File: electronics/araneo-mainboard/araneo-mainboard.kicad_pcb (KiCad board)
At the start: 2 copper layers, 71.5 x 68.5 mm, 97 parts, among them IC1 TPS54302DDCR, IC2 BMI270, IC3 MMC5983MA, J2 OLED, J3 GPIO, SW2 SW, SW3 SW, U4 POWER, U5 PAM8403D, U6 3V3

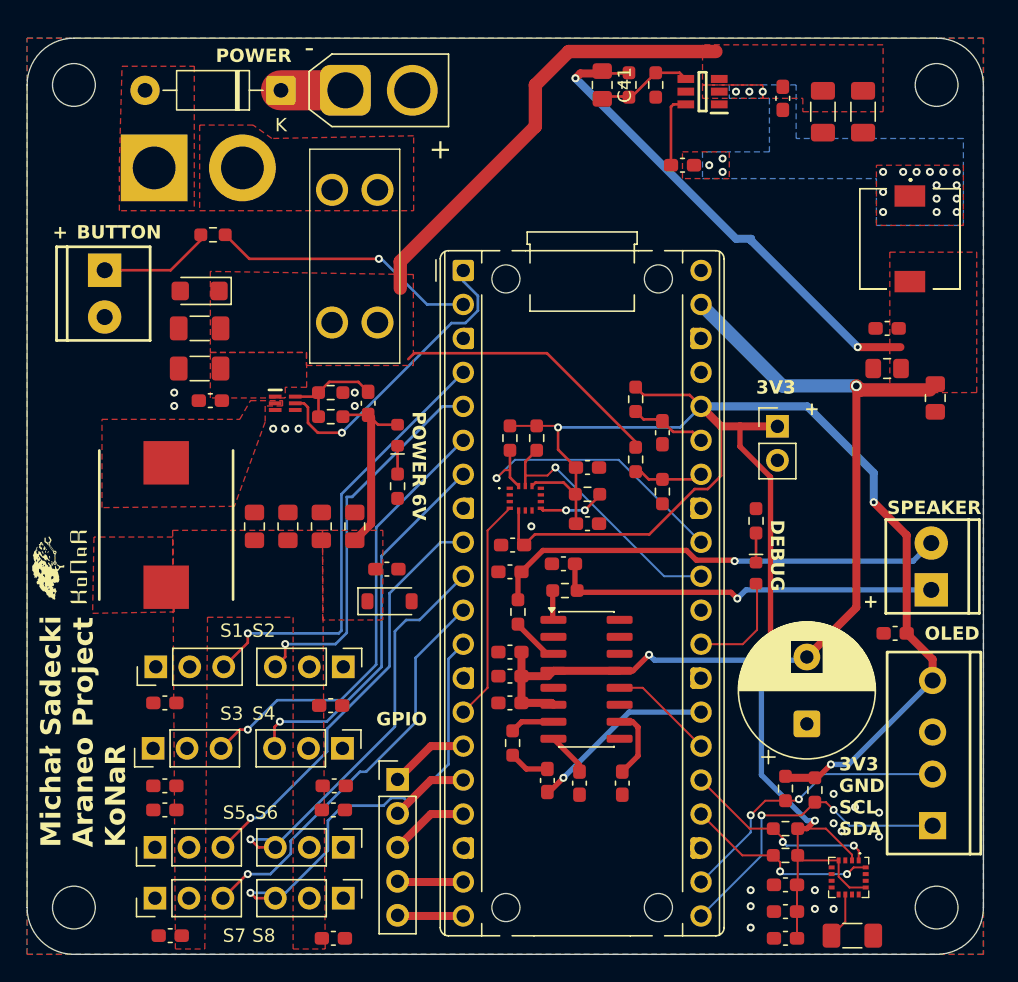
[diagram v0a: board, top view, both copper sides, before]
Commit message: electronics: remove unnecessary capacitors, add net labels, change screw terminal to JST_XH
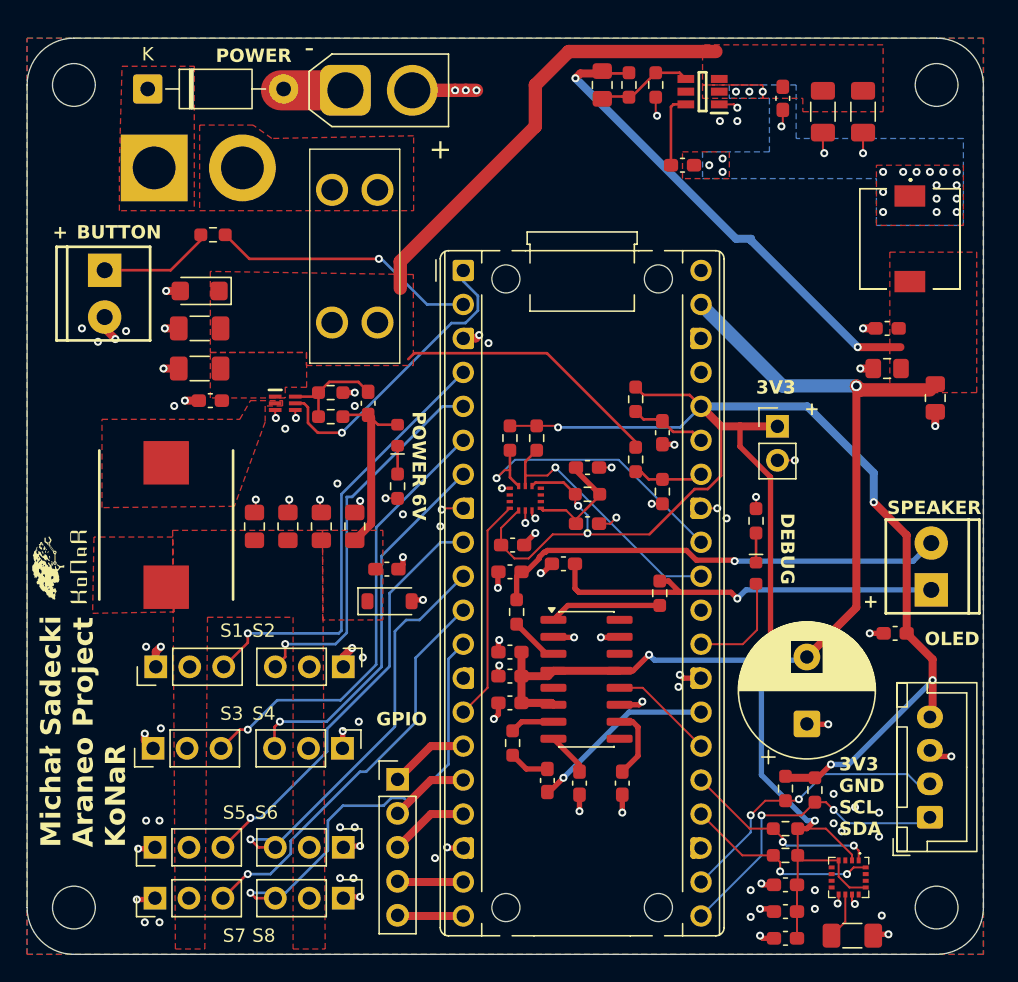
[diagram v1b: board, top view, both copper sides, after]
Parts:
- removed C21, C22, C23, C24, C25, C26, C27, C28: 0.1uF, Capacitor_SMD:C_0603_1608Metric_Pad1.08x0.95mm_HandSolder
- removed FB1, FB2: FerriteBead, Resistor_SMD:R_0603_1608Metric_Pad0.98x0.95mm_HandSolder
- added R20: 0, Resistor_SMD:R_0603_1608Metric_Pad0.98x0.95mm_HandSolder, F.Cu at (138.8, 77.0)
- added R21: 0, Resistor_SMD:R_0603_1608Metric_Pad0.98x0.95mm_HandSolder, F.Cu at (128.1, 78.4)
- J2: footprint PCM_SparkFun-Connector:ScrewTerminal_1x04_P3.5mm_Locking -> Connector_JST:JST_XH_B4B-XH-A_1x04_P2.50mm_Vertical
- R13: value 1.2k -> 1k
- moved D6 9.96 mm to (100.5, 39.3), turned to 0 degrees
- moved J2 0.49 mm to (159.0, 93.8)
- turned C1 to 180 degrees
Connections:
- net Net-(C11-Pad2) renamed /SP_P_O
- net Net-(C12-Pad2) renamed /SP_N_O
- net Net-(C13-Pad2) renamed /INL_R
- net Net-(D3-K) renamed /D_LED
- net Net-(D5-K) renamed /LED6
- net Net-(IC1-BOOT) renamed /BOOT
- net Net-(IC1-FB) renamed /FB5
- net Net-(IC1-SW) renamed /SW5_L
- net Net-(IC3-CAP) renamed /Magnetometer/MAG_CAP
- net Net-(PS1-FB) renamed /FB6
- net Net-(PS1-SW) renamed /SW6_L
- net Net-(SW2-A) renamed /BTN_R
- net Net-(SW3-B) renamed /VBAT_SW
- net Net-(U5-INR) renamed /INR
- net Net-(U5-VREF) renamed /SP_VREF
- C42 pad 2: +3V3 -> /IMU/VDD_IMU
- C43 pad 2: +3V3 -> /IMU/VDD_IMU
- D6 pad 1: +7.4V -> /VBAT_D
- D6 pad 2: Net-(D6-A) -> +7.4V
- FB4 pad 1: Net-(IC2-VDD) -> /IMU/VDD_IMU
- IC2 pad 8: Net-(IC2-VDD) -> /IMU/VDD_IMU
- SW3 pad 1: Net-(D6-A) -> /VBAT_D
- U5 pad 1: Net-(U5-LOUT+) -> /LOUT+
- U5 pad 3: Net-(U5-LOUT-) -> /LOUT-
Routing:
- net GND: track 0.00 -> 81.6 mm, vias 20 -> 106
- net /IMU/VDD_IMU: track 0.00 -> 8.93 mm
- net /LOUT+: track 0.00 -> 8.40 mm
- net Net-(IC2-VDD): track 5.01 -> 0.00 mm, vias 2 -> 0
- net /LOUT-: track 0.00 -> 3.67 mm
- net Net-(U5-LOUT-): track 3.60 -> 0.00 mm
- net Net-(U5-LOUT+): track 2.21 -> 0.00 mm
- net /SP_P_O: track 29.1 -> 30.9 mm
- net +3V3: track 162.5 -> 163.9 mm, vias 5 -> 8
- added copper zone on F.Cu, net /VBAT_D
- removed copper zone on F.Cu, net Net-(D6-A)

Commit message: electronics: change bucks layout
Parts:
- moved konar1 66.7 mm to (152.2, 42.5), turned to 0 degrees
- moved C41 29.2 mm to (161.8, 49.5), turned to 90 degrees
- moved R16 25.3 mm to (159.5, 49.5), turned to -90 degrees
- moved R17 17.2 mm to (154.2, 46.0), turned to 0 degrees
- moved IC1 16.1 mm to (154.2, 50.0), turned to 0 degrees
- moved R14 16.1 mm to (120.0, 57.0), turned to -90 degrees
- moved C20 15.6 mm to (154.0, 52.8), turned to 0 degrees
- moved D6 13.3 mm to (96.4, 52.0)
- moved SW2 13.2 mm to (95.8, 66.0)
- moved SW3 12.8 mm to (98.5, 57.8)
- moved C31 12.1 mm to (100.8, 68.8), turned to -90 degrees
- moved D2 10.3 mm to (106.5, 64.5), turned to 90 degrees
- moved C45 10.2 mm to (114.2, 84.5)
- moved R6 10.0 mm to (114.0, 72.0)
- moved D1 9.93 mm to (114.8, 86.8)
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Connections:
- net /IMU/VDD_IMU renamed /VDD_IMU
- net /Magnetometer/MAG_CAP renamed /MAG_CAP
- net Net-(U5-INL) renamed /INL
- IC2 pad 13: /IMU_SDA -> /IMU_SCL
- IC2 pad 14: /IMU_SCL -> /IMU_SDA
- R1 pad 2: /IMU_SDA -> /IMU_SCL
- R2 pad 2: /IMU_SCL -> /IMU_SDA
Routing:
- net +5V: track 106.9 -> 28.5 mm, vias 4 -> 1
- net +3V3: track 163.9 -> 123.1 mm
- net GND: track 81.6 -> 41.9 mm, vias 106 -> 50
- net +7.4V_F: track 55.1 -> 20.3 mm
- net /BUTTON: track 20.0 -> 0.00 mm, vias 1 -> 0
- net /PWM6: track 30.3 -> 14.0 mm, vias 1 -> 0
- net /PWM8: track 31.9 -> 15.9 mm, vias 1 -> 0
- net /PWM7: track 30.3 -> 15.1 mm, vias 1 -> 0
- net +6V: track 14.4 -> 0.00 mm
- net /PWM3: track 33.7 -> 19.5 mm, vias 1 -> 0
- net /PWM5: track 31.7 -> 19.2 mm, vias 1 -> 0
- net /PWM1: track 33.4 -> 23.1 mm, vias 1 -> 0
- net /BTN_R: track 8.52 -> 0.00 mm
- net /FB6: track 8.01 -> 0.00 mm
- net /PWM2: track 28.6 -> 21.3 mm, vias 1 -> 0
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- removed copper zone on F.Cu, net +5V
- removed copper zone on F.Cu, net +7.4V_F
- removed copper zone on B.Cu, net /SW5_L
- removed copper zone on F.Cu, net /SW5_L
- removed copper zone on F.Cu, net /SW6_L
- removed copper zone on F.Cu, net /VBAT_D
- removed copper zone on F.Cu, net /VBAT_SW
- removed copper zone on B.Cu, net GND
- removed copper zone on F.Cu, net GND
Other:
- board size 71.5 x 68.5 mm -> 71.5 x 63.8 mm

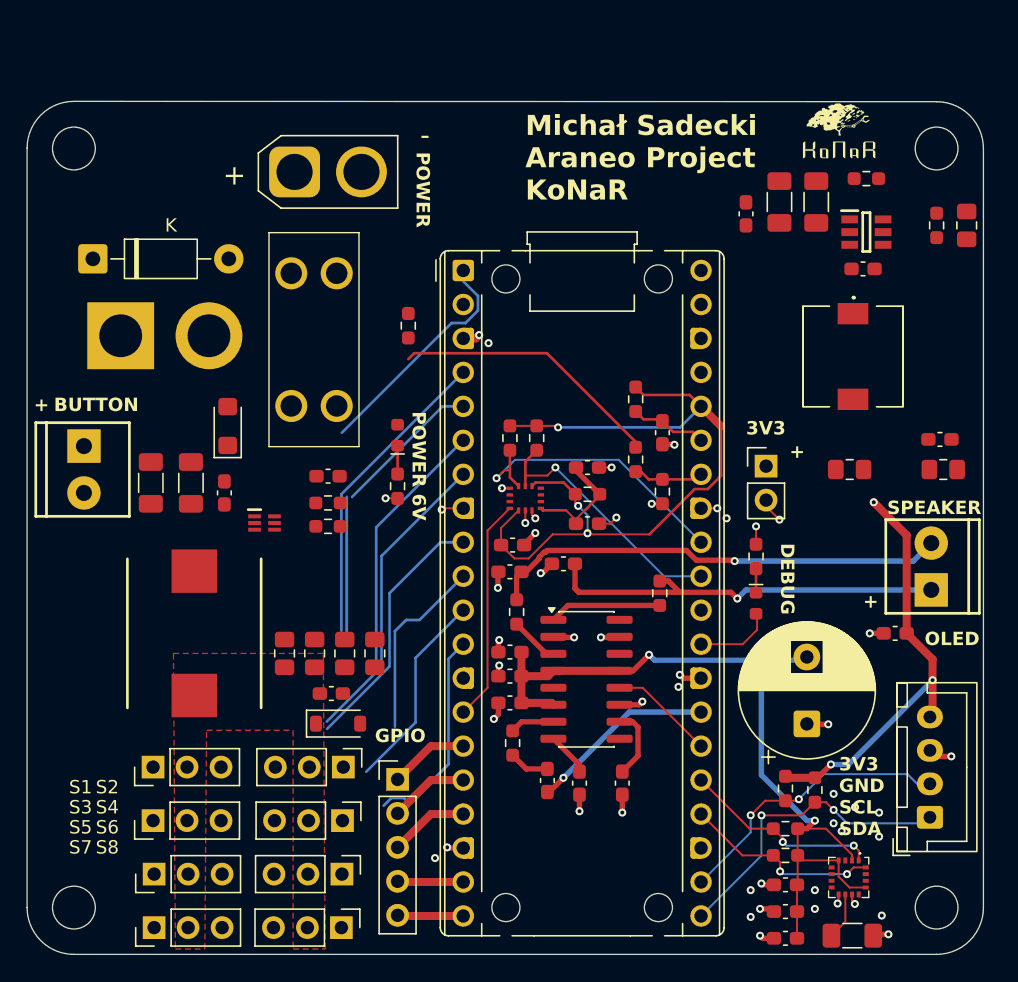
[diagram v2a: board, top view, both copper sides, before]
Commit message: electronics: connect bucks
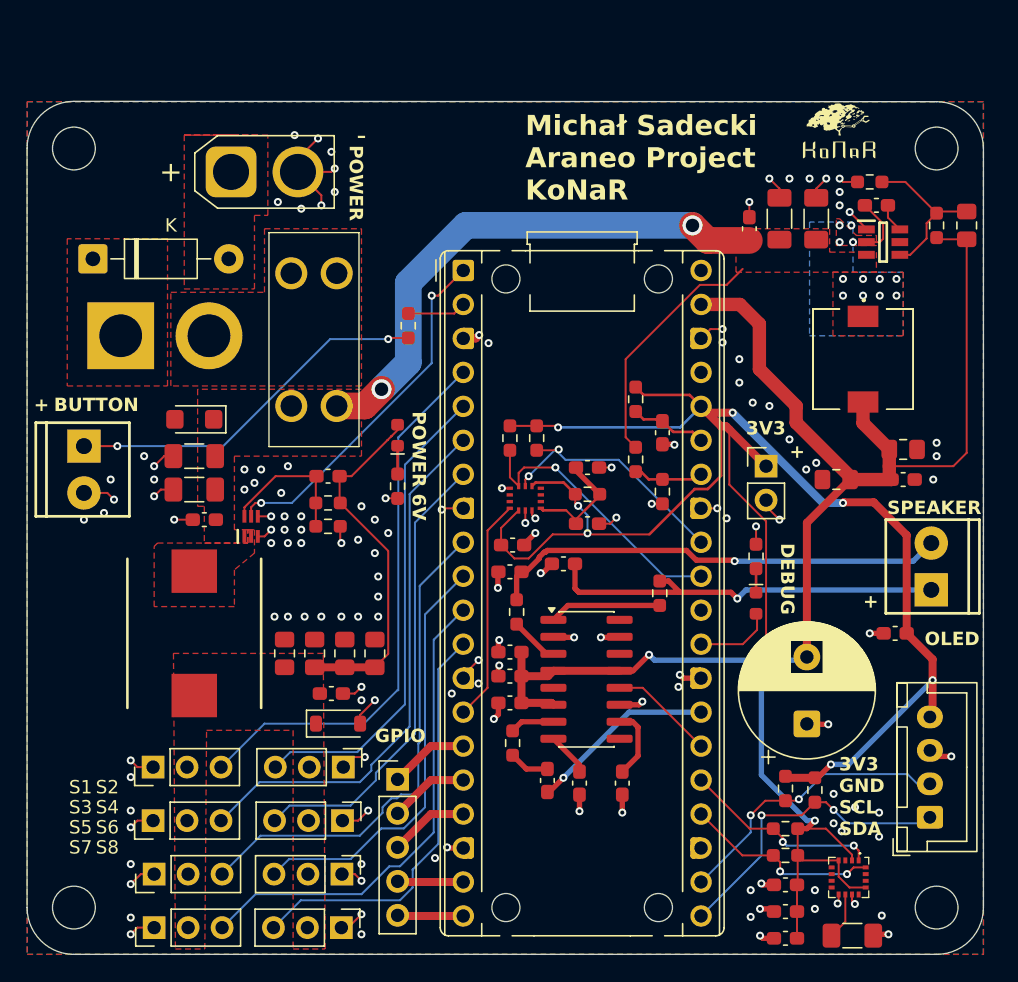
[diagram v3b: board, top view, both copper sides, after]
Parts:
- moved C29 8.04 mm to (152.0, 68.5), turned to 180 degrees
- moved C20 4.85 mm to (155.0, 48.0)
- moved U4 4.75 mm to (106.8, 45.5)
- moved C30 4.27 mm to (157.0, 66.2), turned to 0 degrees
- moved C44 4.07 mm to (157.0, 68.5)
- moved C31 3.82 mm to (104.0, 66.8), turned to 180 degrees
- moved D2 2.55 mm to (104.0, 64.0), turned to 180 degrees
- moved C33 2.50 mm to (104.8, 71.5), turned to 180 degrees
- moved IC1 1.46 mm to (155.5, 50.8)
- moved C39 1.25 mm to (147.8, 49.0)
- moved C40 1.25 mm to (150.5, 49.0)
- moved C35 1.14 mm to (145.5, 49.8)
- moved PS1 1.03 mm to (108.2, 72.0), turned to 90 degrees
- moved L2 0.78 mm to (154.0, 59.5)
- moved C32 0.56 mm to (104.0, 69.2), turned to 180 degrees
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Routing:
- net +5V: track 28.5 -> 97.1 mm
- net GND: track 41.9 -> 92.8 mm, vias 50 -> 138
- net +3V3: track 123.1 -> 162.9 mm, vias 8 -> 9
- net +7.4V_F: track 20.3 -> 58.8 mm, vias 0 -> 2
- net /BTN_R: track 0.00 -> 27.6 mm, vias 0 -> 2
- net +6V: track 0.00 -> 26.9 mm
- net /PWM7: track 15.1 -> 36.3 mm
- net /PWM3: track 19.5 -> 40.3 mm
- net /PWM1: track 23.1 -> 41.4 mm
- net /PWM5: track 19.2 -> 37.4 mm
- net /PWM6: track 14.0 -> 31.8 mm
- net /PWM8: track 15.9 -> 31.4 mm
- net /PWM2: track 21.3 -> 35.7 mm
- net /FB5: track 0.00 -> 12.1 mm
- net /PWM4: track 22.7 -> 34.4 mm
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- added copper zone on F.Cu, net +7.4V
- added copper zone on F.Cu, net +7.4V_F
- added copper zone on B.Cu, net /SW5_L
- added copper zone on F.Cu, net /SW5_L
- added copper zone on F.Cu, net /SW6_L
- added copper zone on F.Cu, net /VBAT_D
- added copper zone on F.Cu, net /VBAT_SW
- added copper zone on B.Cu, net GND
- added copper zone on F.Cu, net GND

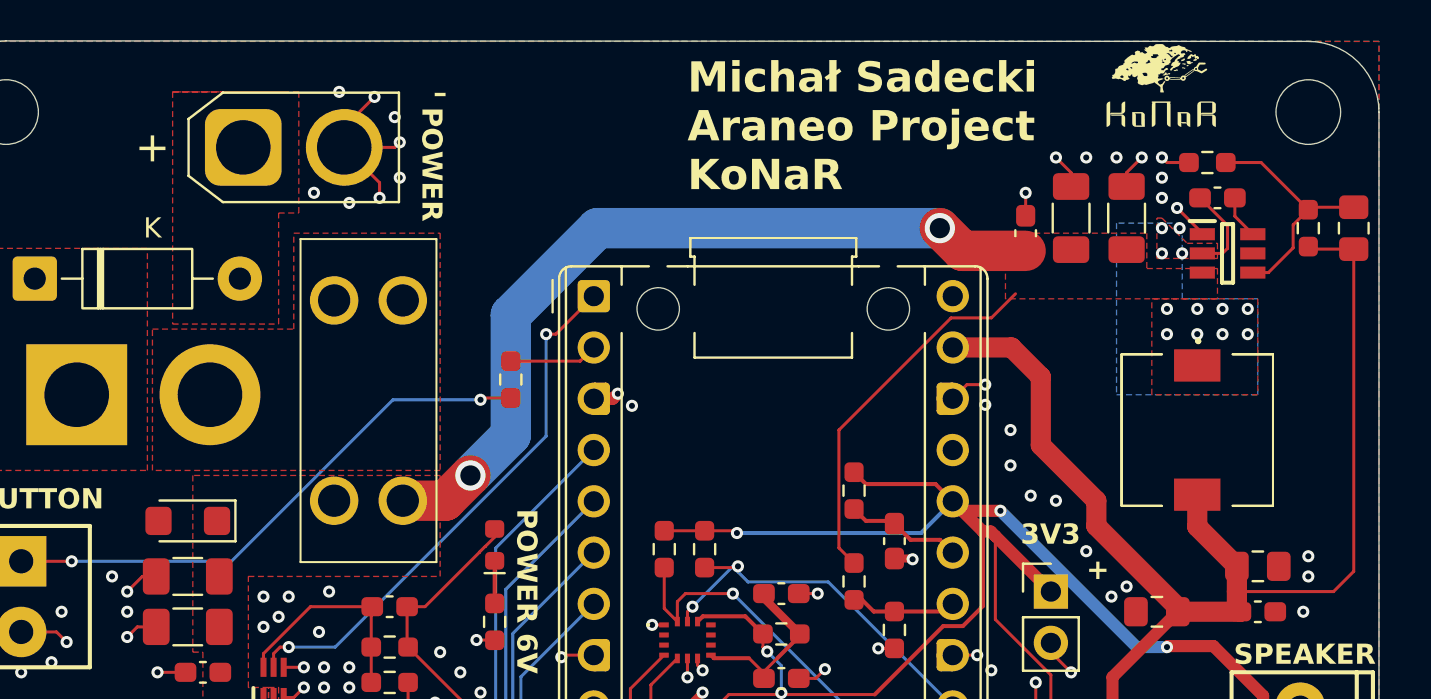
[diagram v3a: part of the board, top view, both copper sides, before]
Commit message: electronics: add vias
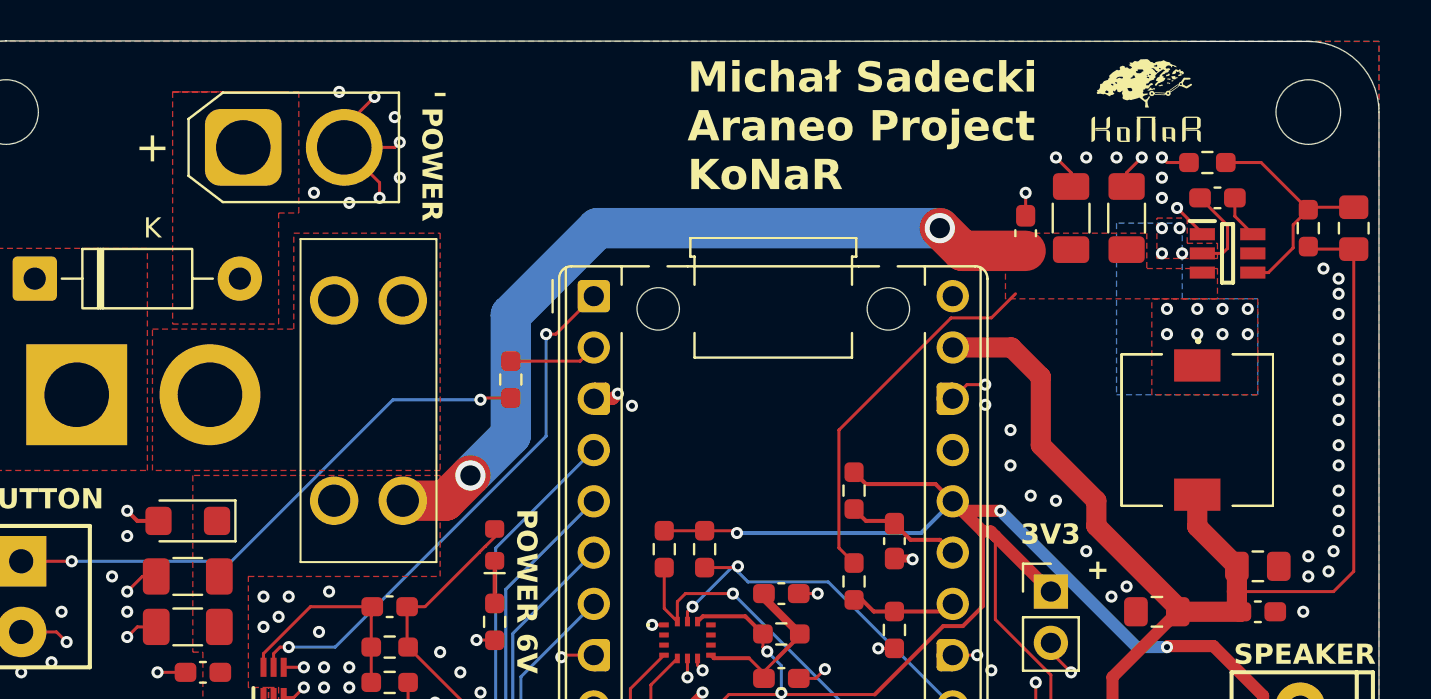
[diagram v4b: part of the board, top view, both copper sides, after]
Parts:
- moved konar1 1.06 mm to (151.5, 43.2)
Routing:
- net GND: track 92.8 -> 94.5 mm, vias 138 -> 156
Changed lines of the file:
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@@
 	(footprint "Custom:konar"
 		(layer "F.Cu")
-		(at 152.25 42.5)
+		(at 151.5 43.25)
 		(property "Reference" "konar1"
 			(at 0 0 0)
@@
 	)
 	(segment
+		(start 102.55 64)
+		(end 101.5 64)
+		(width 0.2)
+		(layer "F.Cu")
+		(net "GND")
+	)
+	(segment
 		(start 135.556587 71.343413)
 		(end 135.1 71.8)
@@
 	)
 	(segment
+		(start 101.5 64)
+		(end 101 63.5)
+		(width 0.2)
+		(layer "F.Cu")
+		(net "GND")
+	)
+	(segment
 		(start 143.1 70.65)
 		(end 141.89 70.65)
@@
 	)
 	(via
+		(at 161 61.25)
+		(size 0.6)
+		(drill 0.3)
+		(layers "F.Cu" "B.Cu")
+		(free yes)
+		(net "GND")
+	)
+	(via
 		(at 123.25 84.5)
 		(size 0.6)
@@
 	)
 	(via
+		(at 161 55)
+		(size 0.6)
+		(drill 0.3)
+		(layers "F.Cu" "B.Cu")
+		(free yes)
+		(net "GND")
+	)
+	(via
 		(at 99.25 94.5)
 		(size 0.6)
@@
 	)
 	(via
+		(at 160.5 66.5)
+		(size 0.6)
+		(drill 0.3)
+		(layers "F.Cu" "B.Cu")
+		(free yes)
+		(net "GND")
+	)
+	(via
+		(at 161 52)
+		(size 0.6)
+		(drill 0.3)
+		(layers "F.Cu" "B.Cu")
+		(free yes)
+		(net "GND")
+	)
+	(via
 		(at 107.75 67.75)
 		(size 0.6)
@@
 	)
 	(via
+		(at 161 59)
+		(size 0.6)
+		(drill 0.3)
+		(layers "F.Cu" "B.Cu")
+		(free yes)
+		(net "GND")
+	)
+	(via
 		(at 117.75 77.25)
 		(size 0.6)
@@
 	)
 	(via
+		(at 161 56)
+		(size 0.6)
+		(drill 0.3)
+		(layers "F.Cu" "B.Cu")
+		(free yes)
+		(net "GND")
+	)
+	(via
 		(at 151.8 92)
 		(size 0.6)
@@
 	)
 	(via
+		(at 160.25 51.5)
+		(size 0.6)
+		(drill 0.3)
+		(layers "F.Cu" "B.Cu")
+		(free yes)
+		(net "GND")
+	)
+	(via
 		(at 129.5 72.5)
 		(size 0.6)
@@
 	)
 	(via
+		(at 161 62.5)
+		(size 0.6)
+		(drill 0.3)
+		(layers "F.Cu" "B.Cu")
+		(free yes)
+		(net "GND")
+	)
+	(via
 		(at 143.1 70.65)
 		(size 0.6)
@@
 	)
 	(via
+		(at 161 64.5)
+		(size 0.6)
+		(drill 0.3)
+		(layers "F.Cu" "B.Cu")
+		(free yes)
+		(net "GND")
+	)
+	(via
 		(at 126.8 82.4)
 		(size 0.6)
@@
 	)
 	(via
+		(at 160.75 65.5)
+		(size 0.6)
+		(drill 0.3)
+		(layers "F.Cu" "B.Cu")
+		(free yes)
+		(net "GND")
+	)
+	(via
 		(at 110.25 47.75)
 		(size 0.6)
@@
 	)
 	(via
+		(at 101 64.75)
+		(size 0.6)
+		(drill 0.3)
+		(layers "F.Cu" "B.Cu")
+		(free yes)
+		(net "GND")
+	)
+	(via
 		(at 116.5 84)
 		(size 0.6)
@@
 	)
 	(via
+		(at 161 63.5)
+		(size 0.6)
+		(drill 0.3)
+		(layers "F.Cu" "B.Cu")
+		(free yes)
+		(net "GND")
+	)
+	(via
 		(at 97.75 68.5)
 		(size 0.6)
@@
 	)
 	(via
+		(at 101 63.5)
+		(size 0.6)
+		(drill 0.3)
+		(layers "F.Cu" "B.Cu")
+		(free yes)
+		(net "GND")
+	)
+	(via
 		(at 151.4 86.8)
 		(size 0.6)
@@
 	)
 	(via
+		(at 161 52.75)
+		(size 0.6)
+		(drill 0.3)
+		(layers "F.Cu" "B.Cu")
+		(free yes)
+		(net "GND")
+	)
+	(via
 		(at 145.6 101.2)
 		(size 0.6)
@@
 	)
 	(via
+		(at 161 57)
+		(size 0.6)
+		(drill 0.3)
+		(layers "F.Cu" "B.Cu")
+		(free yes)
+		(net "GND")
+	)
+	(via
 		(at 116.5 102.5)
 		(size 0.6)
@@
 	)
 	(via
+		(at 161 58)
+		(size 0.6)
+		(drill 0.3)
+		(layers "F.Cu" "B.Cu")
+		(free yes)
+		(net "GND")
+	)
+	(via
 		(at 99.25 89.5)
 		(size 0.6)
@@
 	)
 	(via
+		(at 161 53.75)
+		(size 0.6)
+		(drill 0.3)
+		(layers "F.Cu" "B.Cu")
+		(free yes)
+		(net "GND")
+	)
+	(via
+		(at 161 60.25)
+		(size 0.6)
+		(drill 0.3)
+		(layers "F.Cu" "B.Cu")
+		(free yes)
+		(net "GND")
+	)
+	(via
 		(at 122.5 70.75)
 		(size 0.6)
@@
 		(polygon
 			(pts
-				(xy 153.5 50.25) (xy 155 50.25) (xy 155 51) (xy 152 51) (xy 152 49) (xy 152.25 49)
+				(xy 153.5 50.25) (xy 155 50.25) (xy 155 51) (xy 152 51) (xy 152 49) (xy 153.5 49)
 			)
 		)
